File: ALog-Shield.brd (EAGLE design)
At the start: 53.3 x 78.5 mm, 32 parts

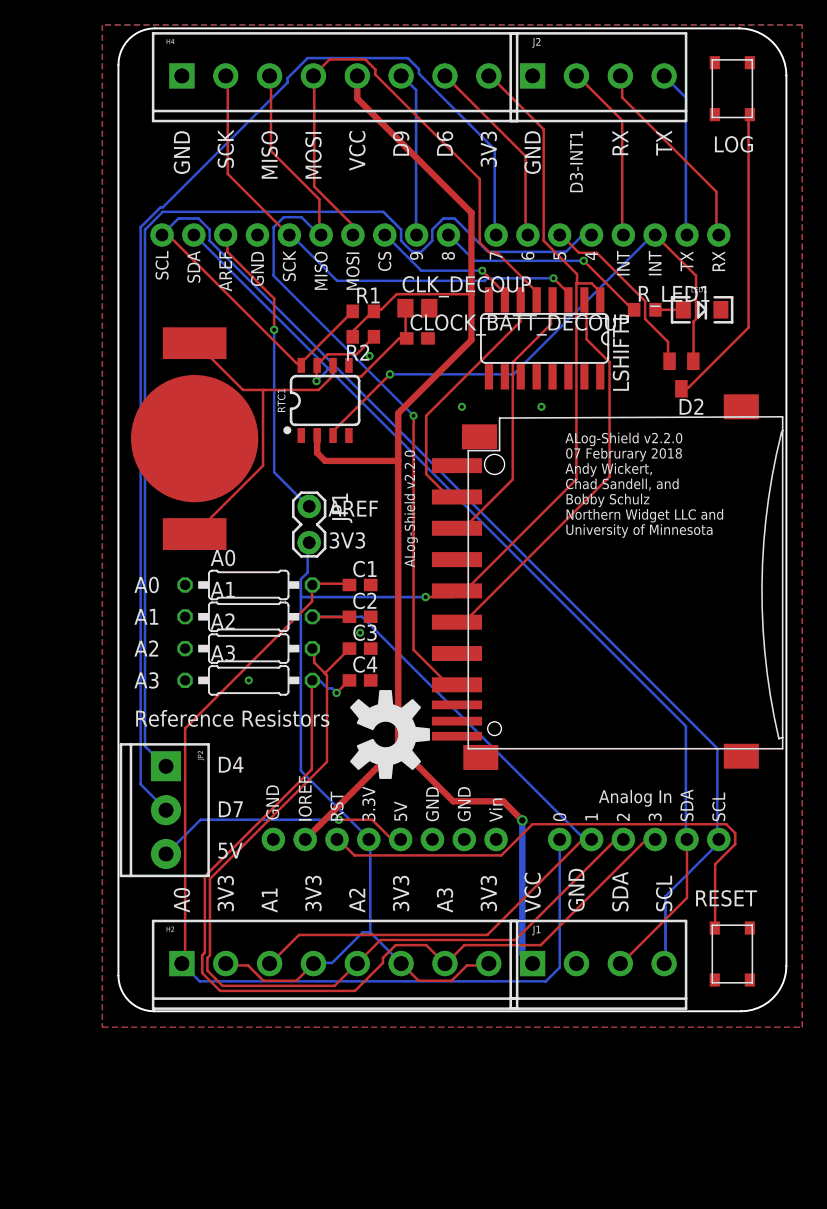
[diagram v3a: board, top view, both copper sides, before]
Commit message: Added final Gerbers for Mrk 2.2.1
Cleaned up routing, fixed button issue, generated gerbers for Mrk 2.2.1
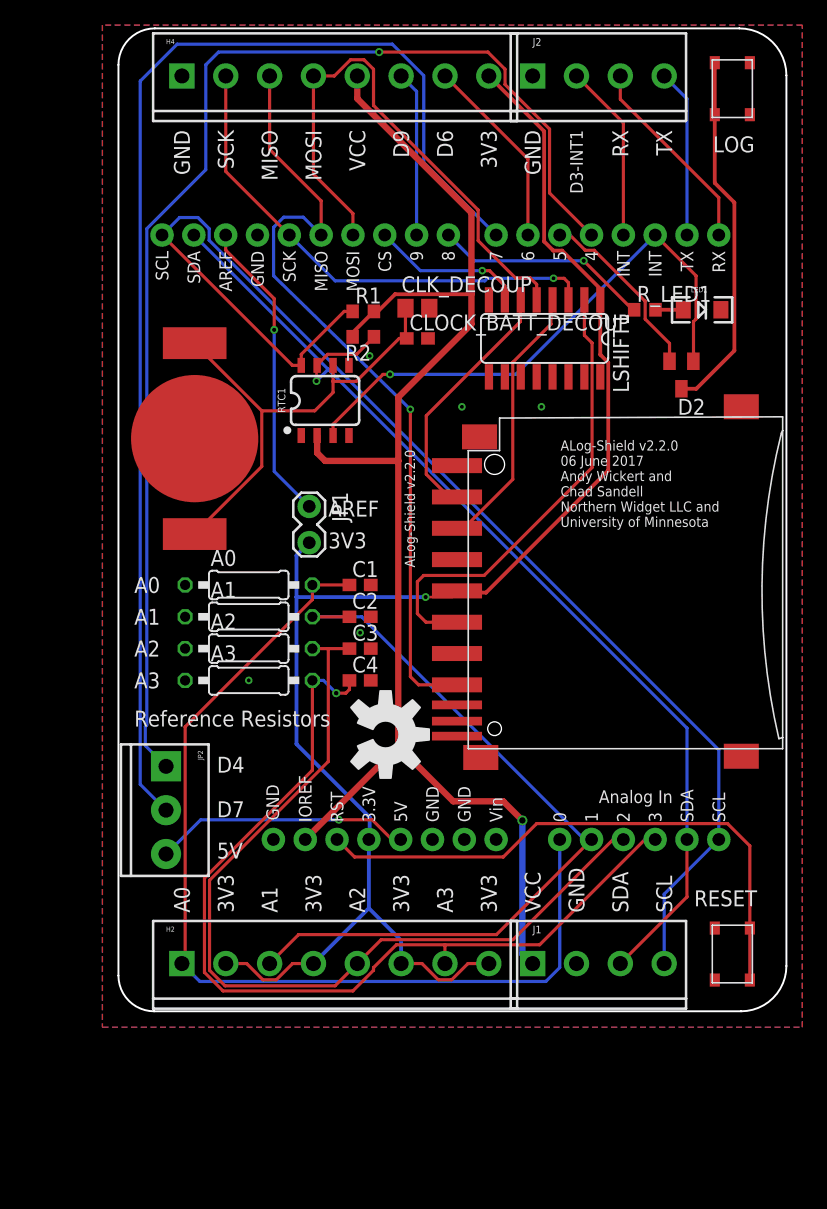
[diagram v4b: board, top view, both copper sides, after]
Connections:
- removed net N$11: D2.3, LOG.2
- new net N$1: D2.3, LOG.3, LOG.4
- net GND: now also LOG.2, RESET.2
- net RESET: now also RESET.3, RESET.4; no longer RESET.2
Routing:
- net N$1: track 0.00 -> 29.1 mm
- net N$11: track 24.5 -> 0.00 mm
- net D4: track 85.0 -> 99.7 mm, vias 0 -> 1
- net D7: track 91.6 -> 99.1 mm
- net SD_CLK: track 32.0 -> 38.2 mm
- net RESET: track 41.9 -> 46.1 mm
- net +3V3: track 123.0 -> 126.7 mm
- net DO: track 62.3 -> 64.5 mm
- net BAT: track 37.4 -> 38.2 mm
